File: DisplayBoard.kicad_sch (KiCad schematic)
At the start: 0 parts

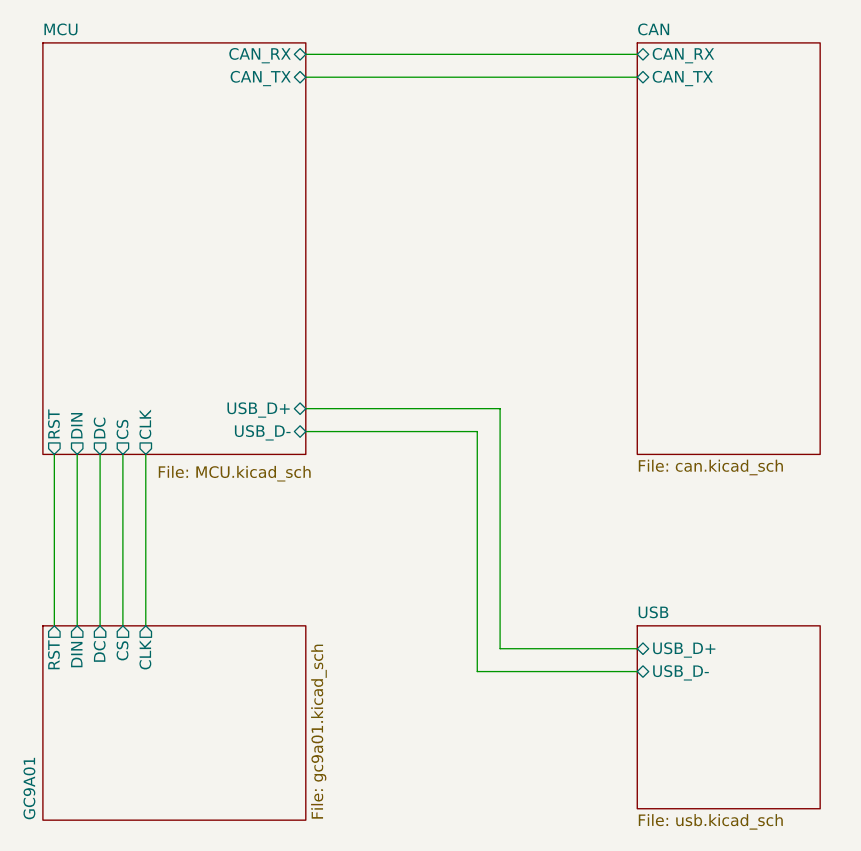
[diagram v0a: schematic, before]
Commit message: Reworked DisplayBoard circuitry and layout; v1.1
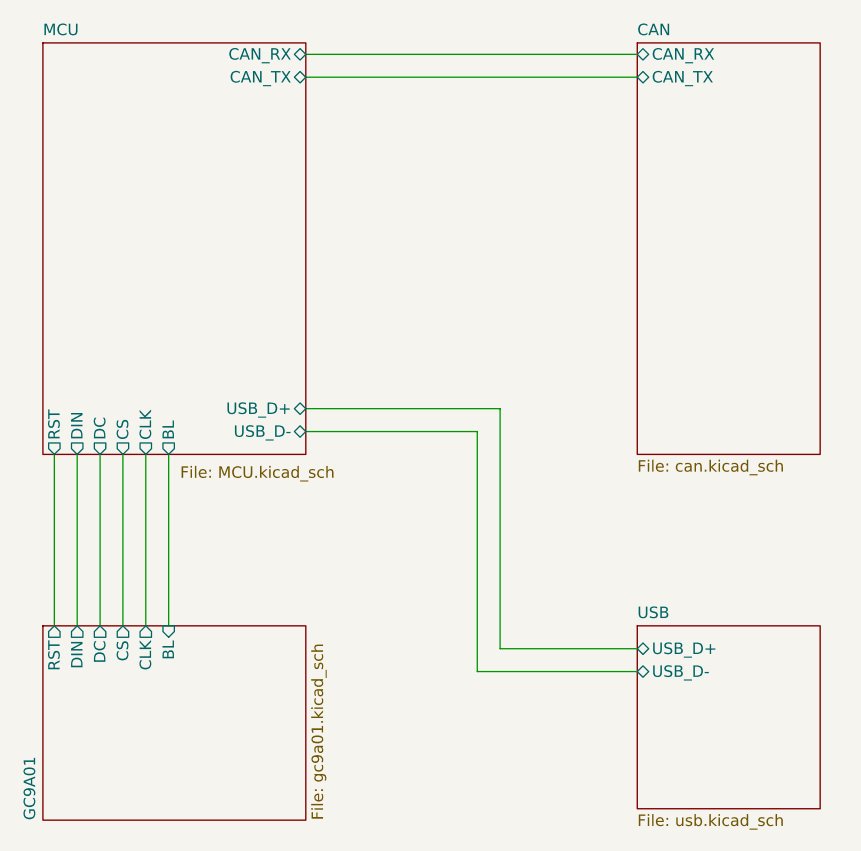
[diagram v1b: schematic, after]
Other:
- sheet GC9A01 ports: added BL; removed none
- sheet MCU ports: added BL; removed none
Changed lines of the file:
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@@
+	(wire
+		(pts
+			(xy 124.46 101.6) (xy 124.46 120.65)
+		)
+		(stroke
+			(width 0)
+			(type default)
+		)
+	)
 	(wire
 		(pts
@@
 			)
 		)
+		(pin "BL" input
+			(at 124.46 120.65 90)
+			(effects
+				(font
+					(size 1.27 1.27)
+				)
+				(justify right)
+			)
+		)
 		(instances
 			(project "DisplayBoard"
@@
 		)
 		(property "Sheetfile" "MCU.kicad_sch"
-			(at 123.19 102.87 0)
+			(at 125.73 102.87 0)
 			(effects
 				(font
@@
 			(effects
 				(font
+					(size 1.27 1.27)
+				)
+				(justify left)
+			)
+		)
+		(pin "BL" output
+			(at 124.46 101.6 270)
+			(effects
+				(font

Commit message: Finished v1.1
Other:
- sheet GC9A01 renamed Display
- sheet Display ports: added IO0, IO1, IO2, IO3, TE; removed DC, DIN
- sheet MCU ports: added IO0, IO1, IO2, IO3, TE; removed DC, DIN
